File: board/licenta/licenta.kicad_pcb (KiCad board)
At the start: 2 copper layers, 36.1 x 36.1 mm, 64 parts, among them IC1 SAMACSYS_PARTS_NCP186BMX330TAG, IC3 SAMACSYS_PARTS_BMI085, J1 SAMACSYS_PARTS_USB4110-GF-A, J2 SAMACSYS_PARTS_112A-TAAR-R03_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, Q1 ESP32_WROVER_SPARKFUN-DISCRET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, Q2 2N7002, SW1 SW_Push, SW2 SW_Push, SW3 SW_Push, SW6 SW_Push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

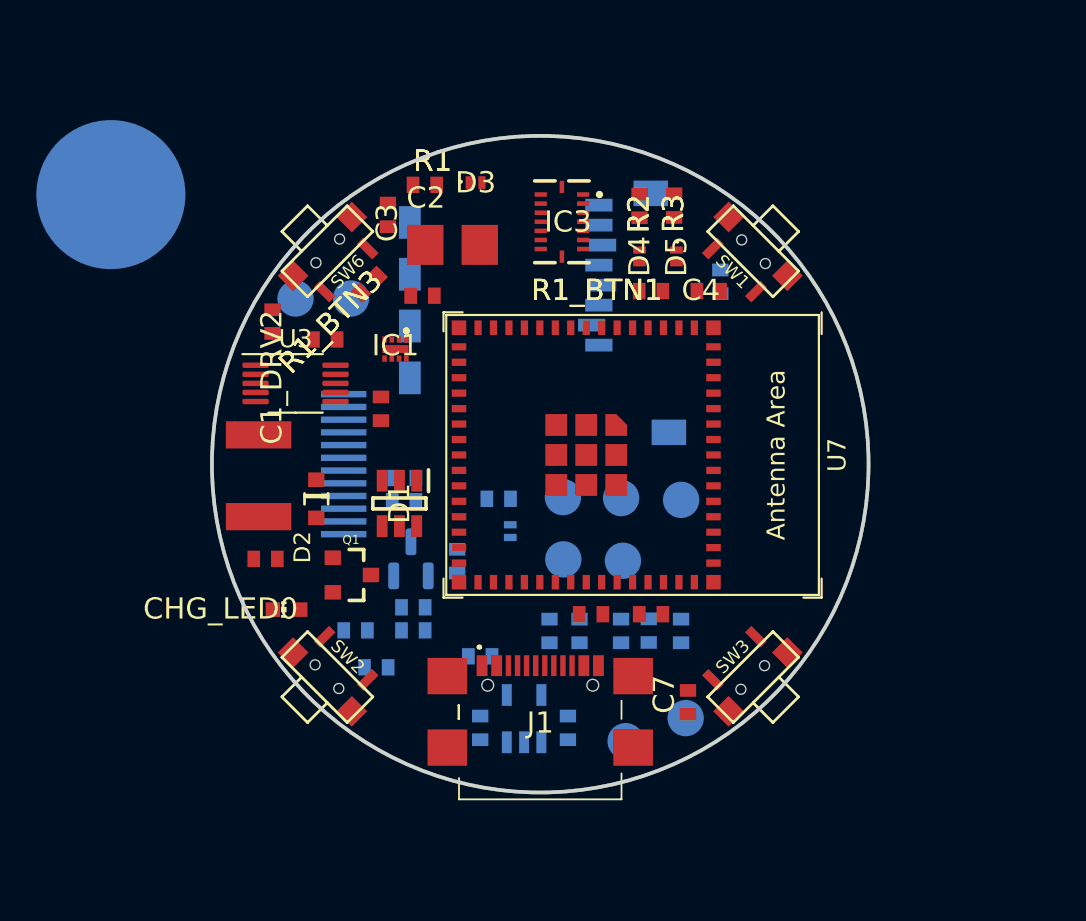
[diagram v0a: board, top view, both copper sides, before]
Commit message: Add DRU and minor pads update
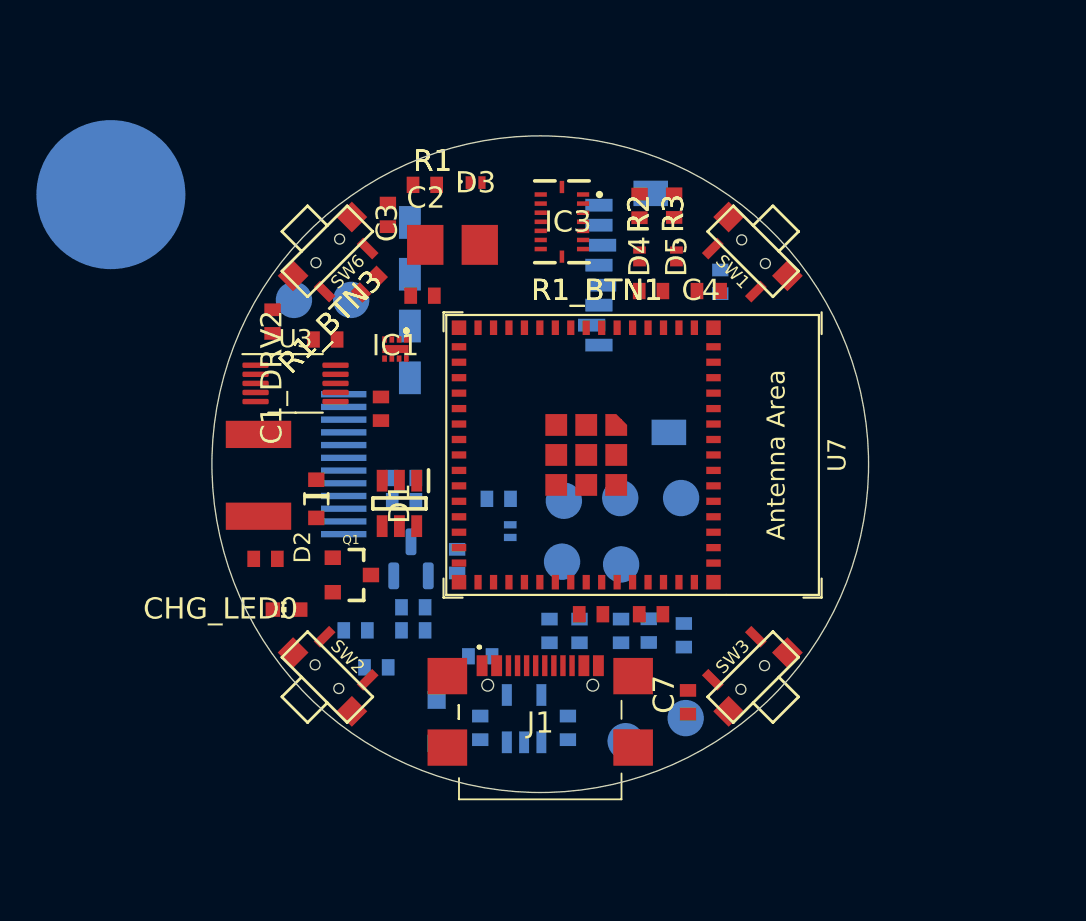
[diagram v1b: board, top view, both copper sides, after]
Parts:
- removed 3V3, GND1, OUT+1, OUT-1, PPG_INT1, SCL1, SDA1: TestPoint, TestPoint:TestPoint_Pad_D2.0mm
- added TP1: OUT+, TestPoint:TestPoint_Pad_D2.0mm, B.Cu at (113.5, 74.5)
- added TP10: VBUS, TestPoint:TestPoint_Pad_1.0x1.0mm, B.Cu at (121.3, 98.9)
- added TP11: VUSB, TestPoint:TestPoint_Pad_1.0x1.0mm, B.Cu at (121.3, 96.5)
- added TP2: OUT-, TestPoint:TestPoint_Pad_D2.0mm, B.Cu at (116.6, 74.5)
- added TP3: 3V3, TestPoint:TestPoint_Pad_D2.0mm, B.Cu at (134.8, 85.4)
- added TP4: SDA, TestPoint:TestPoint_Pad_D2.0mm, B.Cu at (128.3, 85.5)
- added TP5: SCL, TestPoint:TestPoint_Pad_D2.0mm, B.Cu at (131.4, 85.4)
- added TP6: PPG_INT, TestPoint:TestPoint_Pad_D2.0mm, B.Cu at (128.2, 88.9)
- added TP7: GND, TestPoint:TestPoint_Pad_D2.0mm, B.Cu at (131.4, 89.0)
- moved R1_BTN4 0.28 mm to (134.9, 93.0)

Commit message: Add DRC and start routing
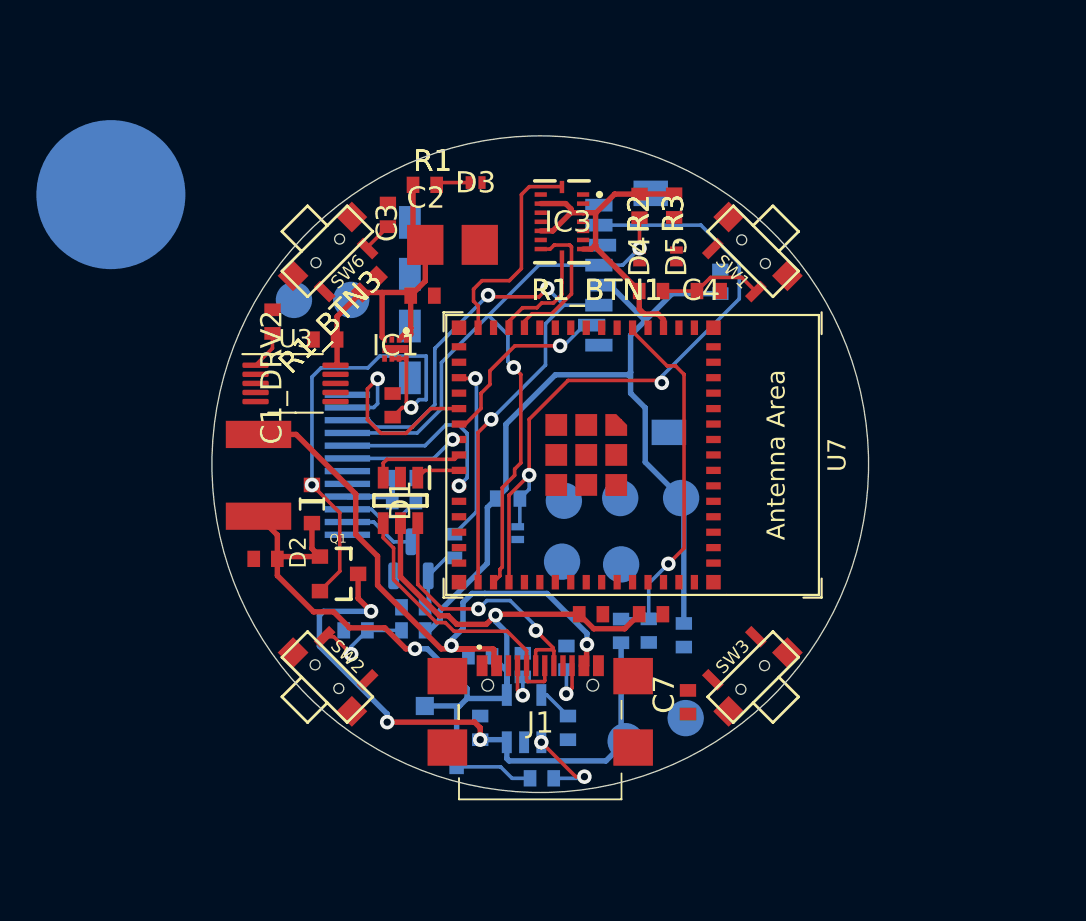
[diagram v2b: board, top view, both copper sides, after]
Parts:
- removed TP11: VUSB, TestPoint:TestPoint_Pad_1.0x1.0mm
- CHG_LED0: moved to B.Cu
- moved CHG_LED0 12.2 mm to (122.4, 99.4), turned to 0 degrees
- moved R1_BAT0 11.0 mm to (127.1, 100.8)
- moved R1_USB0 2.39 mm to (126.0, 94.6)
- moved TP10 2.16 mm to (120.7, 96.8)
- moved R2_USB0 1.65 mm to (128.4, 94.2)
- moved R1_ESP2 0.85 mm to (122.3, 88.0)
- moved Q1 0.71 mm to (115.9, 89.6)
- moved C1_BAT1 0.67 mm to (118.9, 80.3)
- moved R4 0.52 mm to (125.2, 85.4)
- moved D6 0.43 mm to (125.8, 87.3)
- moved D2 0.38 mm to (114.4, 85.7)
- moved U4 0.21 mm to (116.1, 83.6)
- moved D1 0.18 mm to (119.3, 85.5)
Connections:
- U7 pad 1: Net-(U7-GND-Pad1) -> GND
- U7 pad 10: /DISP_RST -> unconnected-(U7-GPIO6/TOUCH6/ADC1_CH5-Pad10)
- U7 pad 11: /IMU_INT -> unconnected-(U7-GPIO7/TOUCH7/ADC1_CH6-Pad11)
- U7 pad 15: /LTR_INT -> /IMU_INT
- U7 pad 2: Net-(U7-GND-Pad1) -> GND
- U7 pad 20: unconnected-(U7-GPIO16/U0CTS/ADC2_CH5/XTAL_32K_N-Pad20) -> /DISP_RST
- U7 pad 21: unconnected-(U7-GPIO17/U1TXD/ADC2_CH6-Pad21) -> /SS_SD
- U7 pad 22: unconnected-(U7-GPIO18/U1RXD/ADC2_CH7/CLK_OUT3-Pad22) -> /TFT_DC
- U7 pad 35: /TX -> unconnected-(U7-MTCK/GPIO39/CLK_OUT3/SUBSPICS1-Pad35)
- U7 pad 36: /RX -> unconnected-(U7-MTDO/GPIO40/CLK_OUT2-Pad36)
- U7 pad 42: Net-(U7-GND-Pad1) -> GND
- U7 pad 43: Net-(U7-GND-Pad1) -> GND
- U7 pad 46: Net-(U7-GND-Pad1) -> GND
- U7 pad 47: Net-(U7-GND-Pad1) -> GND
- U7 pad 48: Net-(U7-GND-Pad1) -> GND
- U7 pad 49: Net-(U7-GND-Pad1) -> GND
- U7 pad 50: Net-(U7-GND-Pad1) -> GND
- U7 pad 51: Net-(U7-GND-Pad1) -> GND
- U7 pad 52: Net-(U7-GND-Pad1) -> GND
- U7 pad 53: Net-(U7-GND-Pad1) -> GND
- U7 pad 54: Net-(U7-GND-Pad1) -> GND
- U7 pad 55: Net-(U7-GND-Pad1) -> GND
- U7 pad 56: Net-(U7-GND-Pad1) -> GND
- U7 pad 57: Net-(U7-GND-Pad1) -> GND
- U7 pad 58: Net-(U7-GND-Pad1) -> GND
- U7 pad 59: Net-(U7-GND-Pad1) -> GND
- U7 pad 6: /TFT_DC -> unconnected-(U7-GPIO2/TOUCH2/ADC1_CH1-Pad6)
- U7 pad 60: Net-(U7-GND-Pad1) -> GND
- U7 pad 61: Net-(U7-GND-Pad1) -> GND
- U7 pad 62: Net-(U7-GND-Pad1) -> GND
- U7 pad 63: Net-(U7-GND-Pad1) -> GND
- U7 pad 64: Net-(U7-GND-Pad1) -> GND
- U7 pad 65: Net-(U7-GND-Pad1) -> GND
- U7 pad 9: /SS_SD -> unconnected-(U7-GPIO5/TOUCH5/ADC1_CH4-Pad9)
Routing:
- net /3V3: track 0.00 -> 90.9 mm
- net /VBUS: track 0.00 -> 53.5 mm, vias 0 -> 2
- net /SCK: track 0.00 -> 39.7 mm, vias 0 -> 2
- net /MISO: track 0.00 -> 38.3 mm, vias 0 -> 2
- net /MOSI: track 0.00 -> 36.6 mm, vias 0 -> 3
- net /VUSB: track 0.00 -> 35.2 mm, vias 0 -> 2
- net /VBAT: track 0.00 -> 33.6 mm, vias 0 -> 3
- net Net-(D2-CATHODE): track 0.00 -> 27.8 mm, vias 0 -> 2
- net /ADC_BAT: track 0.00 -> 19.8 mm, vias 0 -> 1
- net /DN: track 0.00 -> 15.8 mm
- net /DP: track 0.00 -> 15.6 mm, vias 0 -> 2
- net /SS_SD: track 0.00 -> 12.3 mm, vias 0 -> 1
- net /IMU_INT: track 0.00 -> 11.8 mm
- net /DISP_RST: track 0.00 -> 11.5 mm, vias 0 -> 1
- net /SS_TFT: track 0.00 -> 10.3 mm, vias 0 -> 1
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
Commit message: Update components layout and route prototype
Some pins labels on the ESP32 were also modified(BUT NOT THOROUGHLY CHECKED) in order to simplify routing the PCB.
In addition, this commit also provides some screenshots used for documentation.
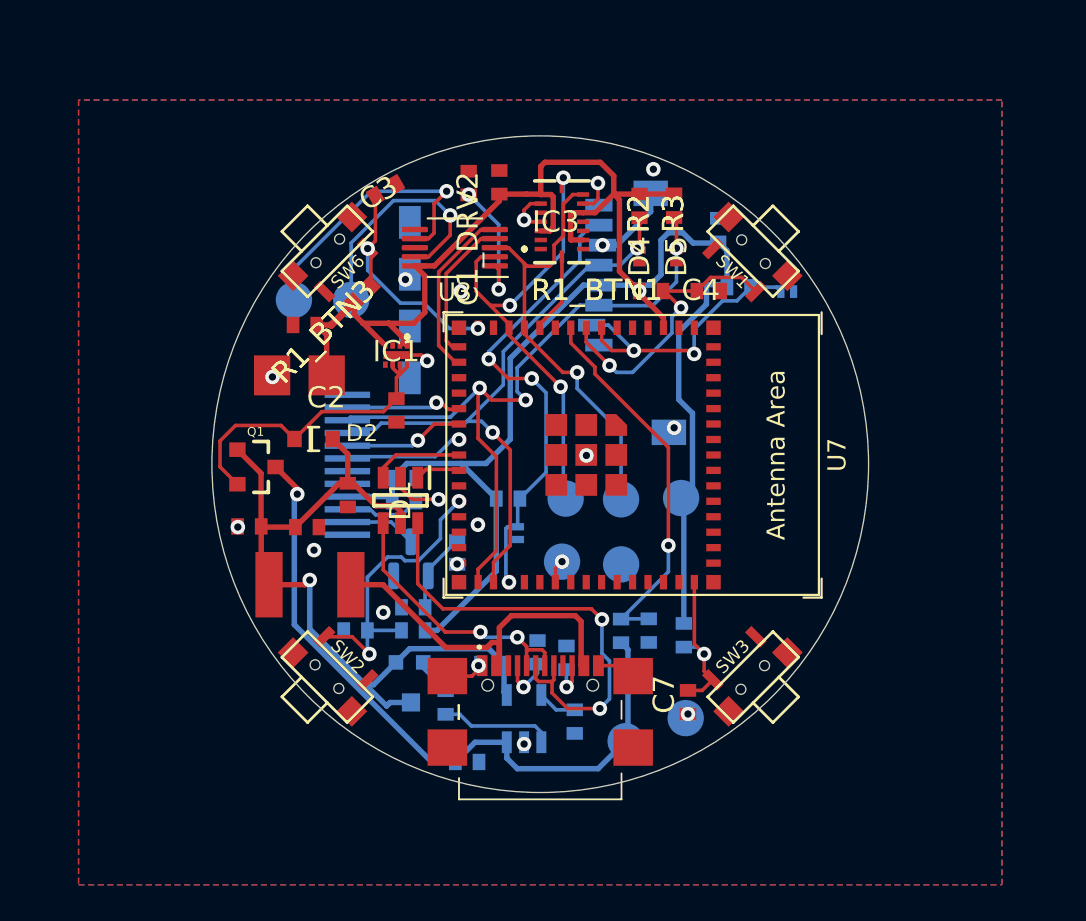
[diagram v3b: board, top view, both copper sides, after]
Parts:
- D3, R1: moved to B.Cu
- moved C2_USB0 22.6 mm to (111.0, 87.0), turned to 180 degrees
- moved R1 18.2 mm to (137.9, 73.8)
- moved D3 18.2 mm to (140.6, 74.0)
- moved C1_USB0 16.3 mm to (114.2, 87.0)
- moved C1_DRV2 13.2 mm to (123.1, 68.1)
- moved C1_DRV1 12.9 mm to (124.8, 68.0), turned to -90 degrees
- moved U3 11.5 mm to (122.3, 71.6), turned to 180 degrees
- moved C2 11.1 mm to (113.8, 78.7), turned to 180 degrees
- moved Q1 7.43 mm to (111.3, 83.7)
- moved R1_BAT0 6.74 mm to (121.8, 96.6), turned to -90 degrees
- moved C1_BAT2 6.67 mm to (114.0, 75.9), turned to 180 degrees
- moved PFMF.050.1 6.65 mm to (114.3, 90.2), turned to 180 degrees
- moved R1_PWRBUS0 5.72 mm to (116.4, 85.2), turned to 90 degrees
- moved CHG_LED0 5.63 mm to (119.8, 94.4), turned to 90 degrees
- moved D2 3.58 mm to (114.5, 82.2), turned to 0 degrees
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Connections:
- U7 pad 11: unconnected-(U7-GPIO7/TOUCH7/ADC1_CH6-Pad11) -> /IMU_INT
- U7 pad 14: /PPG_INT -> unconnected-(U7-GPIO10/TOUCH10/ADC1_CH9/FSPICS0/FSPIIO4/SUBSPICS0-Pad14)
- U7 pad 15: /IMU_INT -> /BUTTON_1
- U7 pad 18: /PIN_LED -> unconnected-(U7-GPIO14/TOUCH14/ADC2_CH3/FSPIWP/FSPIDQS/SUBSPIWP-Pad18)
- U7 pad 21: /SS_SD -> /SS_TFT
- U7 pad 25: /SS_TFT -> unconnected-(U7-GPIO21-Pad25)
- U7 pad 30: unconnected-(U7-GPIO48/SPICLK_N/SUBSPICLK_N_DIFF-Pad30) -> /PIN_LED
- U7 pad 36: unconnected-(U7-MTDO/GPIO40/CLK_OUT2-Pad36) -> /PPG_INT
- U7 pad 5: /ADC_BAT -> unconnected-(U7-GPIO1/TOUCH1/ADC1_CH0-Pad5)
- U7 pad 7: /BUTTON_1 -> /SS_SD
- U7 pad 9: unconnected-(U7-GPIO5/TOUCH5/ADC1_CH4-Pad9) -> /ADC_BAT
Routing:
- net /3V3: track 90.9 -> 118.8 mm, vias 0 -> 1
- net /SCL: track 5.96 -> 26.0 mm, vias 0 -> 3
- net GND: track 0.00 -> 19.0 mm, vias 0 -> 18
- net /SDA: track 7.98 -> 24.1 mm, vias 0 -> 1
- net /OUT+: track 0.00 -> 15.7 mm, vias 0 -> 1
- net /VUSB: track 35.2 -> 21.0 mm, vias 2 -> 0
- net /OUT-: track 0.00 -> 13.4 mm, vias 0 -> 1
- net /MISO: track 38.3 -> 25.8 mm, vias 2 -> 3
- net /BUTTON_1: track 1.66 -> 13.8 mm, vias 0 -> 2
- net /BUTTON_3: track 5.41 -> 16.5 mm, vias 1 -> 2
- net Net-(D2-CATHODE): track 27.8 -> 17.4 mm, vias 2 -> 0
- net /DP: track 15.6 -> 25.9 mm
- net /BUTTON_2: track 5.75 -> 15.8 mm, vias 0 -> 2
- net /PIN_LED: track 10.0 -> 0.14 mm
- net /EN_DRV: track 0.00 -> 9.60 mm
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- added copper zone on B.Cu, net GND
- added copper zone on F.Cu, net GND

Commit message: Update PCB design
This commit changes the button footprints and modifies the silkscreen
of the PCB.
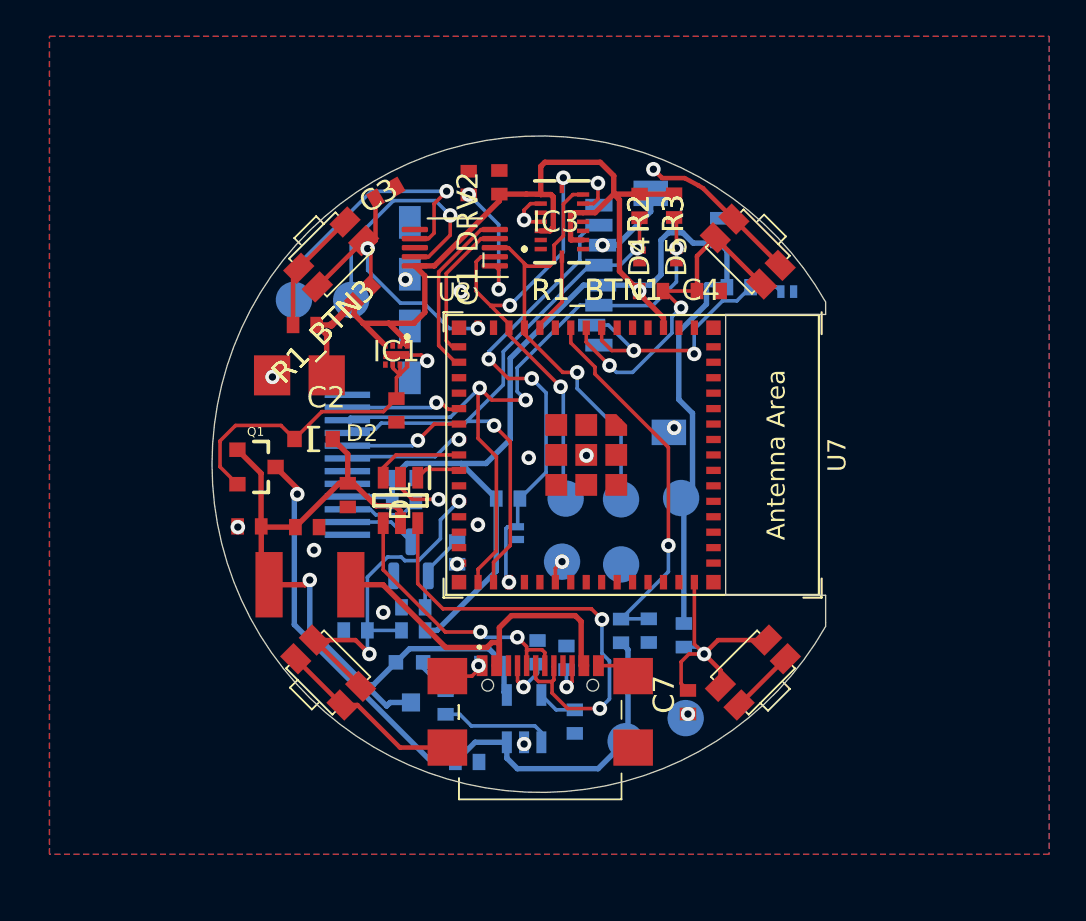
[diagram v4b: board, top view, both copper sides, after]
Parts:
- SW1, SW2, SW3, SW6: footprint open-Smartwatch:button_side_smd -> HW_licenta:EVQ-P7K01P
- moved SW2 1.99 mm to (114.2, 93.6), turned to 135 degrees
- moved SW6 1.89 mm to (116.9, 70.9), turned to 45 degrees
- moved SW3 1.68 mm to (137.3, 96.1), turned to -135 degrees
- moved SW1 1.65 mm to (139.5, 73.3), turned to -45 degrees
- moved C3 0.15 mm to (118.5, 68.6)
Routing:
- net GND: track 19.0 -> 48.9 mm, vias 18 -> 19
- net /RESET: track 8.67 -> 14.8 mm
- net /BUTTON_3: track 16.5 -> 20.6 mm
- net /BUTTON_1: track 13.8 -> 17.9 mm
- net /BUTTON_2: track 15.8 -> 18.9 mm
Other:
- board size 36.1 x 36.1 mm -> 33.8 x 36.1 mm

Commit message: Modify button alignment
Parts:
- moved C3 0.22 mm to (118.7, 68.7)
- moved TP2 0.21 mm to (116.8, 74.6)
- moved TP1 0.21 mm to (113.6, 74.6)
- moved SW1 0.18 mm to (139.6, 73.4)
- moved SW2 0.16 mm to (114.3, 93.7)
- moved TP4 0.16 mm to (131.6, 85.5)
- moved TP7 0.15 mm to (131.4, 88.9)
- moved C7 0.13 mm to (135.0, 96.6)
- moved SW6 0.10 mm to (116.9, 71.0)
- moved R1_BTN3 0.10 mm to (117.3, 74.1)
- moved SW3 0.10 mm to (137.2, 96.1)
- moved TP3 0.10 mm to (134.8, 85.5)
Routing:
- net GND: track 48.9 -> 55.2 mm
- net /RESET: track 14.8 -> 13.1 mm
- net /BUTTON_1: track 17.9 -> 16.5 mm
- net /BUTTON_2: track 18.9 -> 18.0 mm
- net /3V3: track 118.8 -> 119.4 mm
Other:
- board text added: "3V3"
- board text added: "CHG"
- board text added: "GND"
- board text added: "INT"
- board text added: "O+"
- board text added: "O-"
- board text added: "SCL"
- board text added: "SDA"
- board text added: "VBAT"
- board text added: "VBUS"

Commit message: Update PCB and schematics
This commit replaces the LDO and imports new libraries
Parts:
- removed C2: 100uF, mini_iot:RCL_CT3528
- removed IC1: SAMACSYS_PARTS_NCP186BMX330TAG, mini_iot:SAMACSYS_PARTS_NCP186AMX330TAG
- added IC2: ~, mini_iot:XC8107AC20MR-G, F.Cu at (119.0, 77.7)
- C1_BAT1, C1_BAT2: value 4.7uF -> 10uF
- moved C1_BAT1 1.43 mm to (118.0, 81.5)
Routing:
- net /3V3: track 119.4 -> 113.7 mm
- net GND: track 55.2 -> 53.8 mm, vias 19 -> 18
- net Net-(D2-CATHODE): track 17.3 -> 18.1 mm
